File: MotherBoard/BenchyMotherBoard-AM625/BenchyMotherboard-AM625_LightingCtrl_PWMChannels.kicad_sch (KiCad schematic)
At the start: 24 parts, among them J23 B2B-XH-A-M, J28 B2B-XH-A-M, J29 B2B-XH-A-M, J30 B2B-XH-A-M, J31 B2B-XH-A-M, J32 B2B-XH-A-M, Q16 PMXB43UNEZ, Q17 PMXB43UNEZ, Q18 PMXB43UNEZ, Q19 PMXB43UNEZ, Q20 PMXB43UNEZ, Q21 PMXB43UNEZ

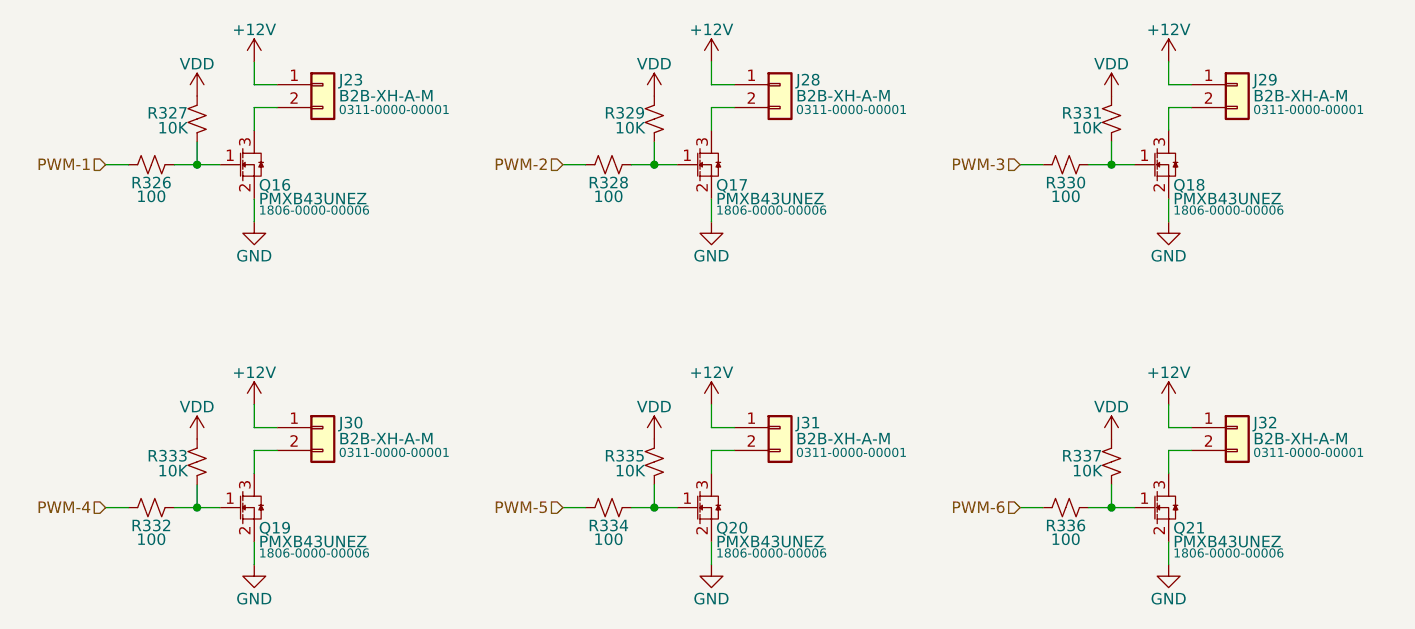
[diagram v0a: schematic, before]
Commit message: Schematic capture mostly complete. Starting PCB layout
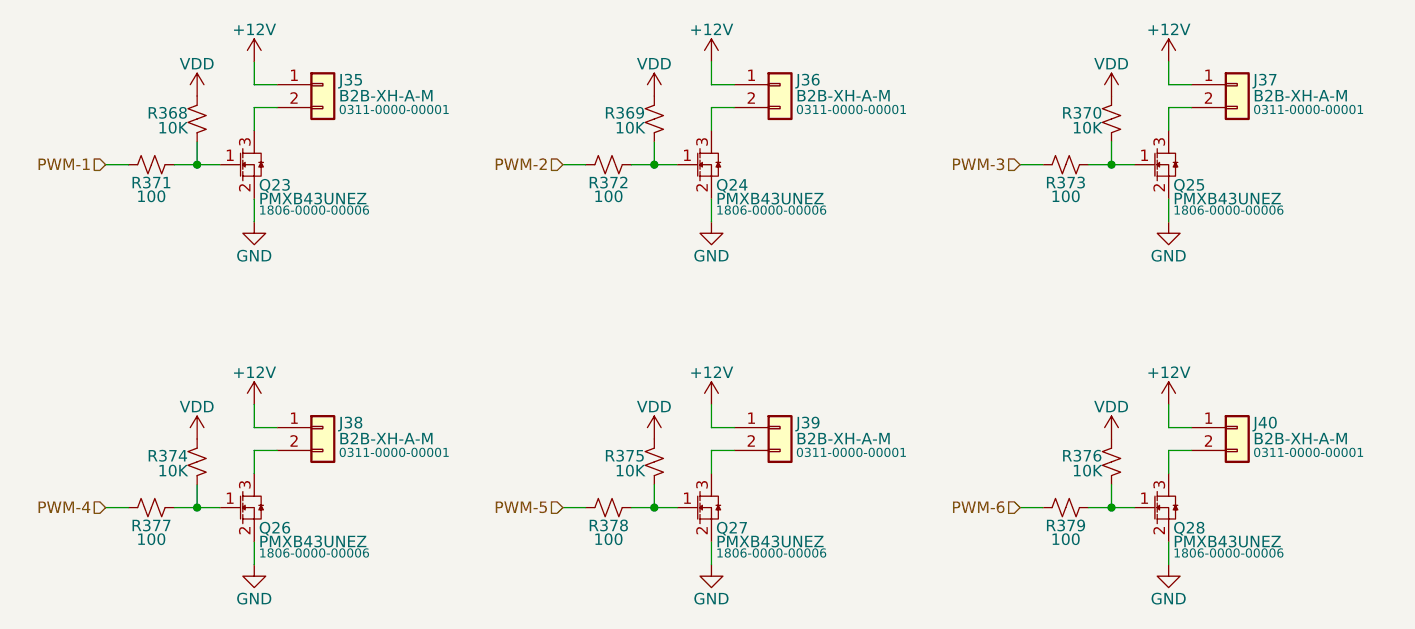
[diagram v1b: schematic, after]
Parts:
- renumbered J23 to J35, J28 to J36, J29 to J37, J30 to J38, J31 to J39, J32 to J40, Q16 to Q23, Q17 to Q24, Q18 to Q25, Q19 to Q26, Q20 to Q27, Q21 to Q28, R327 to R368, R329 to R369, R331 to R370, R326 to R371, R328 to R372, R330 to R373, R333 to R374, R335 to R375, R337 to R376, R332 to R377, R334 to R378, R336 to R379
